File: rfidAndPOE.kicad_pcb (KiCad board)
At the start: 4 copper layers, 100 x 50 mm, 126 parts, among them J1 0813-1X1T-57-F, J2 SWD, J3 MCU Port B, J4 MCU Port C, P1 PoE-, P2 PoE+, P3 GND, P4 +5V, P5 +12V, P6 +3V3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

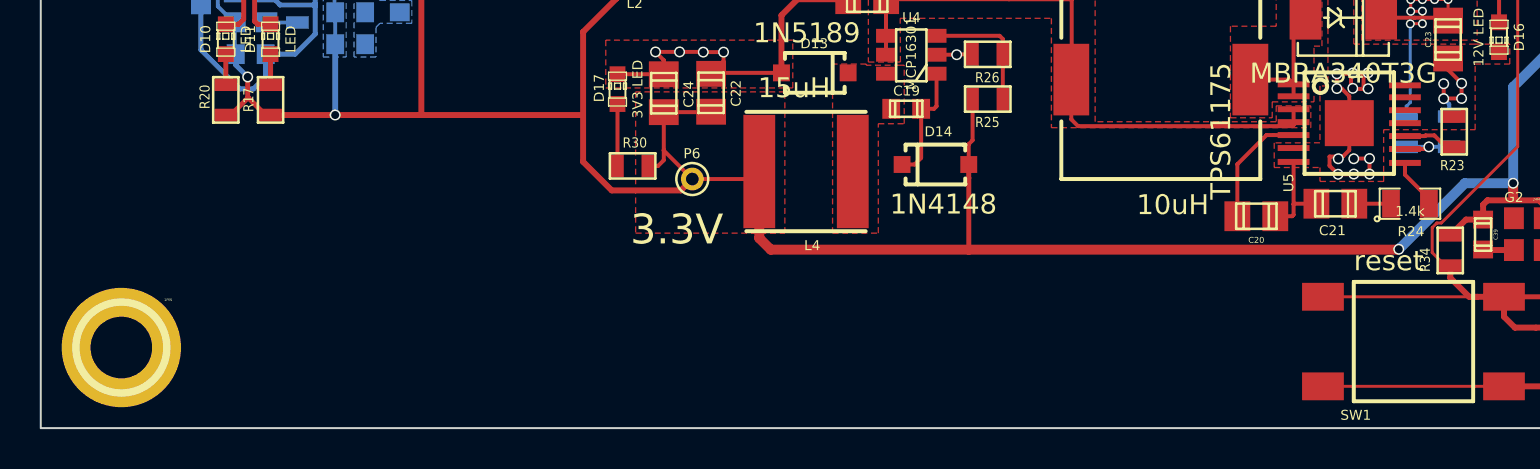
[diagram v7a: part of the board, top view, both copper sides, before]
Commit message: Added OSHW logo (should really be OHW), url for github repo, my name, and number identifiers for each board layer.
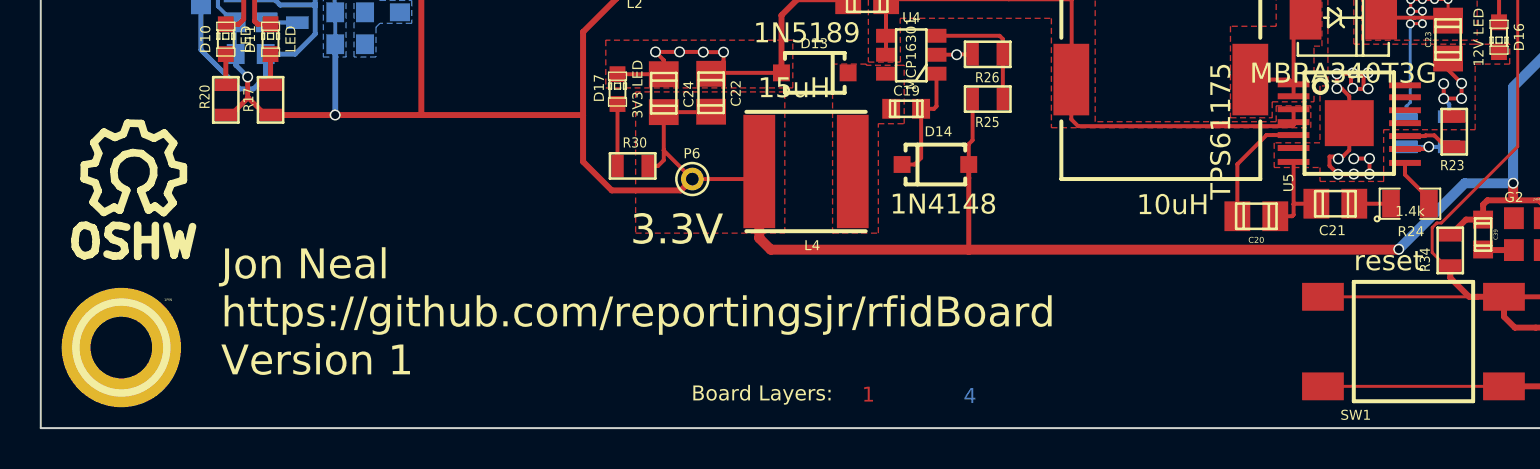
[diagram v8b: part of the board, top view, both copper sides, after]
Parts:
- added SYM: Symbol_OSHW-Logo_SilkScreen_07Jul2012, Symbols:Symbol_OSHW-Logo_SilkScreen, F.Cu at (82.5, 67.8)
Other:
- board text added: "1"
- board text added: "2"
- board text added: "3"
- board text added: "4"
- board text added: "Board Layers:"
- board text added: "Jon Neal https://github.com/reportingsjr/rfidBoard Version 1"
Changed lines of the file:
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@@
 (kicad_pcb (version 4) (host pcbnew "(2014-08-12 BZR 5067)-product")
   (general
-    (links 300)
+    (links 0)
     (no_connects 35)
     (area 72.849999 30.2 177.978572 80.750001)
     (thickness 1.6)
-    (drawings 10)
+    (drawings 16)
     (tracks 1445)
     (zones 0)
-    (modules 126)
+    (modules 127)
     (nets 123)
   )
@@
     (0 F.Cu signal)
     (1 In1.Cu mixed)
-    (2 In2.Cu signal hide)
+    (2 In2.Cu signal)
     (31 B.Cu signal)
     (32 B.Adhes user)
@@
     (pad 1 thru_hole circle (at 0 0) (size 6 6) (drill 3.1) (layers *.Cu *.Mask))
   )
+  (module Symbols:Symbol_OSHW-Logo_SilkScreen (layer F.Cu)
+    (at 82.47 67.85)
+    (descr "Symbol, OSHW-Logo, Silk Screen,")
+    (tags "Symbol, OSHW-Logo, Silk Screen,")
+    (fp_text reference SYM (at 0.09906 -4.38912) (layer F.SilkS) hide
+      (effects (font (thickness 0.3048)))
+    )
+    (fp_text value Symbol_OSHW-Logo_SilkScreen_07Jul2012 (at 0.30988 6.56082) (layer F.SilkS) hide
+      (effects (font (thickness 0.3048)))
+    )
+    (fp_line (start 1.66878 2.68986) (end 2.02946 4.16052) (layer F.SilkS) (width 0.381))
+    (fp_line (start 2.02946 4.16052) (end 2.30886 3.0988) (layer F.SilkS) (width 0.381))
+    (fp_line (start 2.30886 3.0988) (end 2.61874 4.17068) (layer F.SilkS) (width 0.381))
+    (fp_line (start 2.61874 4.17068) (end 2.9591 2.72034) (layer F.SilkS) (width 0.381))
+    (fp_line (start 0.24892 3.38074) (end 1.03886 3.37058) (layer F.SilkS) (width 0.381))
+    (fp_line (start 1.03886 3.37058) (end 1.04902 3.38074) (layer F.SilkS) (width 0.381))
+    (fp_line (start 1.04902 3.38074) (end 1.04902 3.37058) (layer F.SilkS) (width 0.381))
+    (fp_line (start 1.08966 2.65938) (end 1.08966 4.20116) (layer F.SilkS) (width 0.381))
+    (fp_line (start 0.20066 2.64922) (end 0.20066 4.21894) (layer F.SilkS) (width 0.381))
+    (fp_line (start 0.20066 4.21894) (end 0.21082 4.20878) (layer F.SilkS) (width 0.381))
+    (fp_line (start -0.35052 2.75082) (end -0.70104 2.66954) (layer F.SilkS) (width 0.381))
+    (fp_line (start -0.70104 2.66954) (end -1.02108 2.65938) (layer F.SilkS) (width 0.381))
+    (fp_line (start -1.02108 2.65938) (end -1.25984 2.86004) (layer F.SilkS) (width 0.381))
+    (fp_line (start -1.25984 2.86004) (end -1.29032 3.12928) (layer F.SilkS) (width 0.381))
+    (fp_line (start -1.29032 3.12928) (end -1.04902 3.37058) (layer F.SilkS) (width 0.381))
+    (fp_line (start -1.04902 3.37058) (end -0.6604 3.50012) (layer F.SilkS) (width 0.381))
+    (fp_line (start -0.6604 3.50012) (end -0.48006 3.66014) (layer F.SilkS) (width 0.381))
+    (fp_line (start -0.48006 3.66014) (end -0.43942 3.95986) (layer F.SilkS) (width 0.381))
+    (fp_line (start -0.43942 3.95986) (end -0.67056 4.18084) (layer F.SilkS) (width 0.381))
+    (fp_line (start -0.67056 4.18084) (end -0.9906 4.20878) (layer F.SilkS) (width 0.381))
+    (fp_line (start -0.9906 4.20878) (end -1.34112 4.09956) (layer F.SilkS) (width 0.381))
+    (fp_line (start -2.37998 2.64922) (end -2.6289 2.66954) (layer F.SilkS) (width 0.381))
+    (fp_line (start -2.6289 2.66954) (end -2.8702 2.91084) (layer F.SilkS) (width 0.381))
+    (fp_line (start -2.8702 2.91084) (end -2.9591 3.40106) (layer F.SilkS) (width 0.381))
+    (fp_line (start -2.9591 3.40106) (end -2.93116 3.74904) (layer F.SilkS) (width 0.381))
+    (fp_line (start -2.93116 3.74904) (end -2.7305 4.06908) (layer F.SilkS) (width 0.381))
+    (fp_line (start -2.7305 4.06908) (end -2.47904 4.191) (layer F.SilkS) (width 0.381))
+    (fp_line (start -2.47904 4.191) (end -2.16916 4.11988) (layer F.SilkS) (width 0.381))
+    (fp_line (start -2.16916 4.11988) (end -1.95072 3.93954) (layer F.SilkS) (width 0.381))
+    (fp_line (start -1.95072 3.93954) (end -1.8796 3.4798) (layer F.SilkS) (width 0.381))
+    (fp_line (start -1.8796 3.4798) (end -1.9304 3.07086) (layer F.SilkS) (width 0.381))
+    (fp_line (start -1.9304 3.07086) (end -2.03962 2.78892) (layer F.SilkS) (width 0.381))
+    (fp_line (start -2.03962 2.78892) (end -2.4003 2.65938) (layer F.SilkS) (width 0.381))
+    (fp_line (start -1.78054 0.92964) (end -2.03962 1.49098) (layer F.SilkS) (width 0.381))
+    (fp_line (start -2.03962 1.49098) (end -1.50114 2.00914) (layer F.SilkS) (width 0.381))
+    (fp_line (start -1.50114 2.00914) (end -0.98044 1.7399) (layer F.SilkS) (width 0.381))
+    (fp_line (start -0.98044 1.7399) (end -0.70104 1.89992) (layer F.SilkS) (width 0.381))
+    (fp_line (start 0.73914 1.8796) (end 1.06934 1.6891) (layer F.SilkS) (width 0.381))
+    (fp_line (start 1.06934 1.6891) (end 1.50876 2.0193) (layer F.SilkS) (width 0.381))
+    (fp_line (start 1.50876 2.0193) (end 1.9812 1.52908) (layer F.SilkS) (width 0.381))
+    (fp_line (start 1.9812 1.52908) (end 1.69926 1.04902) (layer F.SilkS) (width 0.381))
+    (fp_line (start 1.69926 1.04902) (end 1.88976 0.57912) (layer F.SilkS) (width 0.381))
+    (fp_line (start 1.88976 0.57912) (end 2.49936 0.39116) (layer F.SilkS) (width 0.381))
+    (fp_line (start 2.49936 0.39116) (end 2.49936 -0.28956) (layer F.SilkS) (width 0.381))
+    (fp_line (start 2.49936 -0.28956) (end 1.94056 -0.42926) (layer F.SilkS) (width 0.381))
+    (fp_line (start 1.94056 -0.42926) (end 1.7399 -1.00076) (layer F.SilkS) (width 0.381))
+    (fp_line (start 1.7399 -1.00076) (end 2.00914 -1.47066) (layer F.SilkS) (width 0.381))
+    (fp_line (start 2.00914 -1.47066) (end 1.53924 -1.9812) (layer F.SilkS) (width 0.381))
+    (fp_line (start 1.53924 -1.9812) (end 1.02108 -1.71958) (layer F.SilkS) (width 0.381))
+    (fp_line (start 1.02108 -1.71958) (end 0.55118 -1.92024) (layer F.SilkS) (width 0.381))
+    (fp_line (start 0.55118 -1.92024) (end 0.381 -2.46126) (layer F.SilkS) (width 0.381))
+    (fp_line (start 0.381 -2.46126) (end -0.30988 -2.47904) (layer F.SilkS) (width 0.381))
+    (fp_line (start -0.30988 -2.47904) (end -0.5207 -1.9304) (layer F.SilkS) (width 0.381))
+    (fp_line (start -0.5207 -1.9304) (end -0.9398 -1.76022) (layer F.SilkS) (width 0.381))
+    (fp_line (start -0.9398 -1.76022) (end -1.49098 -2.02946) (layer F.SilkS) (width 0.381))
+    (fp_line (start -1.49098 -2.02946) (end -2.00914 -1.50114) (layer F.SilkS) (width 0.381))
+    (fp_line (start -2.00914 -1.50114) (end -1.76022 -0.96012) (layer F.SilkS) (width 0.381))
+    (fp_line (start -1.76022 -0.96012) (end -1.9304 -0.48006) (layer F.SilkS) (width 0.381))
+    (fp_line (start -1.9304 -0.48006) (end -2.47904 -0.381) (layer F.SilkS) (width 0.381))
+    (fp_line (start -2.47904 -0.381) (end -2.4892 0.32004) (layer F.SilkS) (width 0.381))
+    (fp_line (start -2.4892 0.32004) (end -1.9304 0.5207) (layer F.SilkS) (width 0.381))
+    (fp_line (start -1.9304 0.5207) (end -1.7907 0.91948) (layer F.SilkS) (width 0.381))
+    (fp_line (start 0.35052 0.89916) (end 0.65024 0.7493) (layer F.SilkS) (width 0.381))
+    (fp_line (start 0.65024 0.7493) (end 0.8509 0.55118) (layer F.SilkS) (width 0.381))
+    (fp_line (start 0.8509 0.55118) (end 1.00076 0.14986) (layer F.SilkS) (width 0.381))
+    (fp_line (start 1.00076 0.14986) (end 1.00076 -0.24892) (layer F.SilkS) (width 0.381))
+    (fp_line (start 1.00076 -0.24892) (end 0.8509 -0.59944) (layer F.SilkS) (width 0.381))
+    (fp_line (start 0.8509 -0.59944) (end 0.39878 -0.94996) (layer F.SilkS) (width 0.381))
+    (fp_line (start 0.39878 -0.94996) (end -0.0508 -1.00076) (layer F.SilkS) (width 0.381))
+    (fp_line (start -0.0508 -1.00076) (end -0.44958 -0.89916) (layer F.SilkS) (width 0.381))
+    (fp_line (start -0.44958 -0.89916) (end -0.8509 -0.55118) (layer F.SilkS) (width 0.381))
+    (fp_line (start -0.8509 -0.55118) (end -1.00076 -0.09906) (layer F.SilkS) (width 0.381))
+    (fp_line (start -1.00076 -0.09906) (end -0.94996 0.39878) (layer F.SilkS) (width 0.381))
+    (fp_line (start -0.94996 0.39878) (end -0.70104 0.70104) (layer F.SilkS) (width 0.381))
+    (fp_line (start -0.70104 0.70104) (end -0.35052 0.89916) (layer F.SilkS) (width 0.381))
+    (fp_line (start -0.35052 0.89916) (end -0.70104 1.89992) (layer F.SilkS) (width 0.381))
+    (fp_line (start 0.35052 0.89916) (end 0.7493 1.89992) (layer F.SilkS) (width 0.381))
+  )
+  (gr_text 4 (at 124.51 79.09) (layer B.Cu)
+    (effects (font (size 0.75 0.75) (thickness 0.1875)))
+  )
+  (gr_text 3 (at 122.89 79.03) (layer In2.Cu)
+    (effects (font (size 0.75 0.75) (thickness 0.1875)))
+  )
+  (gr_text 2 (at 121.07 79.01) (layer In1.Cu)
+    (effects (font (size 0.75 0.75) (thickness 0.1875)))
+  )
+  (gr_text 1 (at 119.4 79.02) (layer F.Cu)
+    (effects (font (size 0.75 0.75) (thickness 0.1875)))
+  )
+  (gr_text "Board Layers:" (at 114.06 78.96) (layer F.SilkS)
+    (effects (font (size 0.75 0.75) (thickness 0.1875)))
+  )
+  (gr_text "Jon Neal\nhttps://github.com/reportingsjr/rfidBoard\nVersion 1" (at 86.86 74.89) (layer F.SilkS)
+    (effects (font (size 1.5 1.5) (thickness 0.3)) (justify left))
+  )
   (gr_text 3.3V (at 109.77 70.72) (layer F.SilkS)
     (effects (font (size 1.5 1.5) (thickness 0.3)))
@@
         (xy 134.95 32.05) (xy 134.95 52.8) (xy 111.35 52.8) (xy 109.85 52.8) (xy 109.85 46.35)
         (xy 109.85 46.2) (xy 87.3 46.2) (xy 85.8 47.05) (xy 84.35 47.8) (xy 84.35 63.75)
-        (xy 78.5 63.75) (xy 78.5 80) (xy 177.25 80) (xy 177.2 31.5) (xy 134.95 31.5)
+        (xy 78.5 63.75) (xy 78.5 80) (xy 109.204365 80) (xy 109.2 78) (xy 125.6 78)
+        (xy 125.6 80) (xy 177.25 80) (xy 177.2 31.5) (xy 134.95 31.5)
       )
     )
